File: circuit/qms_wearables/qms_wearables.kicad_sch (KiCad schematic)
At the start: 5 parts, among them P1 SEN-11574, U1 ESP32-DEVKIT-V1, U2 module_mpu6050

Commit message: wip: First draft complete kiosk circuit.
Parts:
- removed Power_Source1: Conn_01x02_Pin, symbol Connector:Conn_01x02_Pin
- removed Vibration_Motor_Module1: Conn_01x03_Pin, symbol Connector:Conn_01x03_Pin
- added BT1: BK-18650-PC4, BK-18650-PC4:BAT_BK-18650-PC4, symbol BK-18650-PC4:BK-18650-PC4
- added P2: PWM VIBRATION MOTOR, SEN_11574:XDCR_SEN-11574, symbol SEN-11574:SEN-11574
- added S1: EG1218, DPST_slide_switch:SW_EG1218, symbol DPST_slide_switch:EG1218
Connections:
- net +3.3V: now also P2.2 (V+)
- net GND: now also BT1.1-, P2.3 (GND)
- net at U1.15 (D23): now also P2.1 (SIGNAL)
- net at U1.17 (VP): no longer P1.1 (SIGNAL)
- net at U1.19 (D34): now also P1.1 (SIGNAL)
- net +5V: no longer names the net of U1.30 (VIN)
- net +5V: now also BT1.2+
- new net: BT1.1+, S1.1
- new net: BT1.2-, S1.2
- no-connect marks 0 -> 1

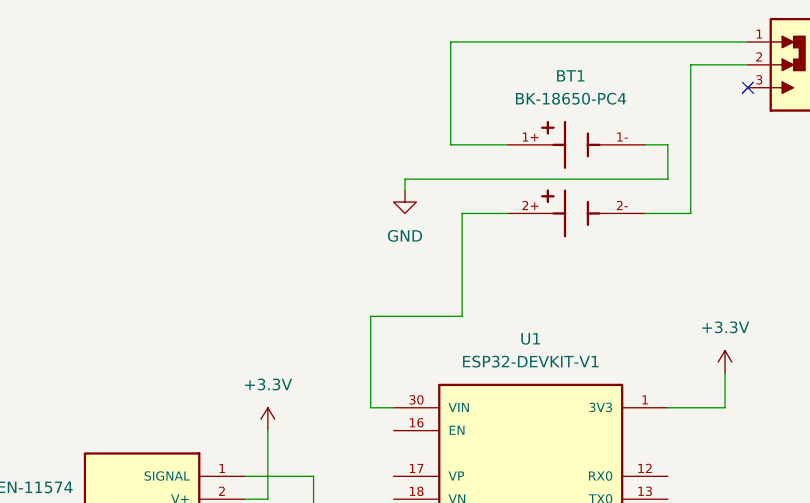
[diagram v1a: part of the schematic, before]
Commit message: wip: First draft complete wearable circuit schematic and pcb with adding 2x battery, DC vibration motor module.
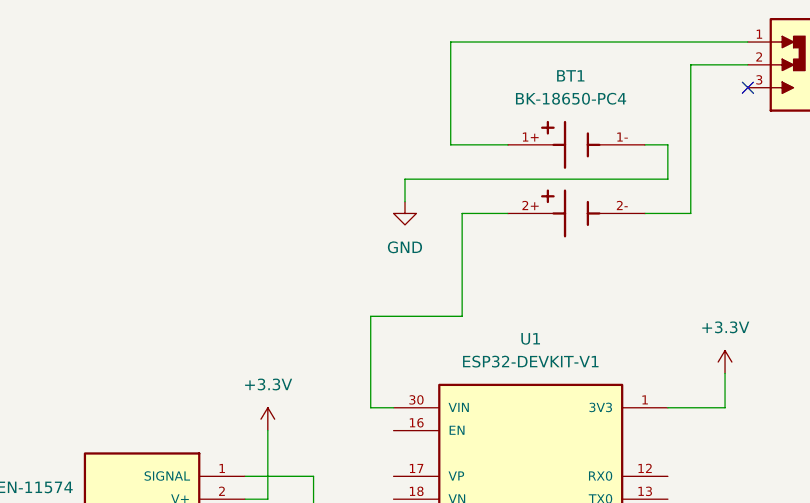
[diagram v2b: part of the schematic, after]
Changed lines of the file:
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@@
 	(wire
 		(pts
-			(xy 105.41 40.64) (xy 105.41 41.91)
+			(xy 105.41 40.64) (xy 105.41 43.18)
 		)
 		(stroke
@@
 	(symbol
 		(lib_id "power:GND")
-		(at 105.41 41.91 0)
+		(at 105.41 43.18 0)
 		(unit 1)
 		(exclude_from_sim no)
@@
 		(fields_autoplaced yes)
 		(property "Reference" "#PWR07"
+			(at 105.41 49.53 0)
+			(effects
+				(font
+					(size 1.27 1.27)
+				)
+				(hide yes)
+			)
+		)
+		(property "Value" "GND"
 			(at 105.41 48.26 0)
 			(effects
@@
 					(size 1.27 1.27)
 				)
-				(hide yes)
-			)
-		)
-		(property "Value" "GND"
-			(at 105.41 46.99 0)
-			(effects
-				(font
-					(size 1.27 1.27)
-				)
 			)
 		)
 		(property "Footprint" ""
-			(at 105.41 41.91 0)
+			(at 105.41 43.18 0)
 			(effects
 				(font
@@
 		)
 		(property "Datasheet" ""
-			(at 105.41 41.91 0)
+			(at 105.41 43.18 0)
 			(effects
 				(font
@@
 		)
 		(property "Description" "Power symbol creates a global label with name \"GND\" , ground"
-			(at 105.41 41.91 0)
-			(effects
-				(font
+			(at 105.41 43.18 0)
+			(effects
+				(font

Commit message: wip: Second draft with replacing the schematic and footprint of vibration motor module
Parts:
- removed P2: PWM VIBRATION MOTOR, SEN_11574:XDCR_SEN-11574, symbol SEN-11574:SEN-11574
- added P2: Vibration Motor Module, Vibration_Motor_Module:XDCR_Vibration_Motor_Module, symbol Vibration_Motor_Module:Vibration_Motor_Module
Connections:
- net +3.3V: now also P2.2 (V+)
- net GND: now also P2.3 (GND)
- net at U1.15 (D23): now also P2.1 (SIGNAL)
- no-connect marks 1 -> 27
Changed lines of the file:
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@@
 	(paper "A4")
 	(no_connect
+		(at 104.14 68.58)
+	)
+	(no_connect
+		(at 104.14 73.66)
+	)
+	(no_connect
+		(at 104.14 99.06)
+	)
+	(no_connect
 		(at 143.51 30.48)
 	)
+	(no_connect
+		(at 134.62 73.66)
+	)
+	(no_connect
+		(at 134.62 76.2)
+	)
+	(no_connect
+		(at 104.14 106.68)
+	)
+	(no_connect
+		(at 134.62 104.14)
+	)
+	(no_connect
+		(at 104.14 93.98)
+	)
+	(no_connect
+		(at 134.62 106.68)
+	)
+	(no_connect
+		(at 104.14 76.2)
+	)
+	(no_connect
+		(at 104.14 104.14)
+	)
+	(no_connect
+		(at 163.83 110.49)
+	)
+	(no_connect
+		(at 134.62 96.52)
+	)
+	(no_connect
+		(at 163.83 107.95)
+	)
+	(no_connect
+		(at 104.14 88.9)
+	)
+	(no_connect
+		(at 134.62 93.98)
+	)
+	(no_connect
+		(at 104.14 91.44)
+	)
+	(no_connect
+		(at 134.62 101.6)
+	)
+	(no_connect
+		(at 163.83 105.41)
+	)
+	(no_connect
+		(at 134.62 81.28)
+	)
+	(no_connect
+		(at 134.62 83.82)
+	)
+	(no_connect
+		(at 104.14 101.6)
+	)
+	(no_connect
+		(at 104.14 109.22)
+	)
+	(no_connect
+		(at 134.62 99.06)
+	)
+	(no_connect
+		(at 104.14 96.52)
+	)
+	(no_connect
+		(at 163.83 113.03)
+	)
 	(wire
 		(pts
@@
 	(wire
 		(pts
-			(xy 80.01 101.6) (xy 83.82 101.6)
+			(xy 77.47 101.6) (xy 83.82 101.6)
 		)
 		(stroke
@@
 	(wire
 		(pts
-			(xy 80.01 99.06) (xy 90.17 99.06)
+			(xy 77.47 99.06) (xy 90.17 99.06)
 		)
 		(stroke
@@
 	(wire
 		(pts
-			(xy 80.01 104.14) (xy 83.82 104.14)
+			(xy 77.47 104.14) (xy 83.82 104.14)
 		)
 		(stroke
@@
 	)
 	(symbol
-		(lib_id "SEN-11574:SEN-11574")
-		(at 74.93 101.6 180)
-		(unit 1)
-		(exclude_from_sim no)
-		(in_bom yes)
-		(on_board yes)
-		(dnp no)
-		(fields_autoplaced yes)
-		(property "Reference" "P2"
-			(at 68.58 91.44 0)
-			(effects
-				(font
-					(size 1.27 1.27)
-				)
-			)
-		)
-		(property "Value" "PWM VIBRATION MOTOR"
-			(at 68.58 93.98 0)
-			(effects
-				(font
-					(size 1.27 1.27)
-				)
-			)
-		)
-		(property "Footprint" "SEN_11574:XDCR_SEN-11574"
-			(at 74.93 101.6 0)
-			(effects
-				(font
-					(size 1.27 1.27)
-				)
-				(justify bottom)
-				(hide yes)
-			)
-		)
-		(property "Datasheet" ""
-			(at 74.93 101.6 0)
-			(effects
-				(font
-					(size 1.27 1.27)
-				)
-				(hide yes)
-			)
-		)
-		(property "Description" ""
-			(at 74.93 101.6 0)
-			(effects
-				(font
-					(size 1.27 1.27)
-				)
-				(hide yes)
-			)
-		)
-		(property "MANUFACTURER" "Sparkfun Electronics"
-			(at 74.93 101.6 0)
-			(effects
-				(font
-					(size 1.27 1.27)
-				)
-				(justify bottom)
-				(hide yes)
-			)
-		)
-		(pin "1"
-		)
-		(pin "3"
-		)
-		(pin "2"
-		)
-		(instances
-			(project "qms_wearables"
-				(path "/81221e85-c470-4436-ab82-7fff3486476b"
-					(reference "P2")
-					(unit 1)
-				)
-			)
-		)
-	)
-	(symbol
 		(lib_id "ESP32-DEVKIT-V1:ESP32-DEVKIT-V1")
 		(at 119.38 91.44 0)
@@
 					(unit 1)
 				)
+			)
+		)
+	)
+	(symbol
+		(lib_id "Vibration_Motor_Module:Vibration_Motor_Module")
+		(at 72.39 101.6 180)
+		(unit 1)
+		(exclude_from_sim no)
+		(in_bom yes)
+		(on_board yes)
+		(dnp no)
+		(fields_autoplaced yes)
+		(property "Reference" "P2"
+			(at 66.04 91.44 0)
+			(effects
+				(font
+					(size 1.27 1.27)
+				)
+			)
+		)
+		(property "Value" "Vibration Motor Module"
+			(at 66.04 93.98 0)
+			(effects
+				(font
+					(size 1.27 1.27)
+				)
+			)
+		)
+		(property "Footprint" "Vibration_Motor_Module:XDCR_Vibration_Motor_Module"
+			(at 64.262 110.49 0)
+			(effects
+				(font
+					(size 1.27 1.27)
+				)
+				(justify bottom)
+				(hide yes)
+			)
+		)
+		(property "Datasheet" ""
+			(at 72.39 101.6 0)
+			(effects
+				(font
+					(size 1.27 1.27)
+				)
+				(hide yes)
+			)
+		)
+		(property "Description" ""
+			(at 72.39 101.6 0)
+			(effects
+				(font
+					(size 1.27 1.27)
+				)
+				(hide yes)
+			)
+		)
+		(property "MANUFACTURER" "Sparkfun Electronics"
+			(at 72.39 101.6 0)
+			(effects
+				(font
+					(size 1.27 1.27)
+				)
+				(justify bottom)
+				(hide yes)
+			)
+		)
+		(pin "1"
+		)
+		(pin "2"
+		)
+		(pin "3"
+		)
+		(instances
+			(project ""
+				(path "/81221e85-c470-4436-ab82-7fff3486476b"
+					(reference "P2")
+					(unit 1)
+				)

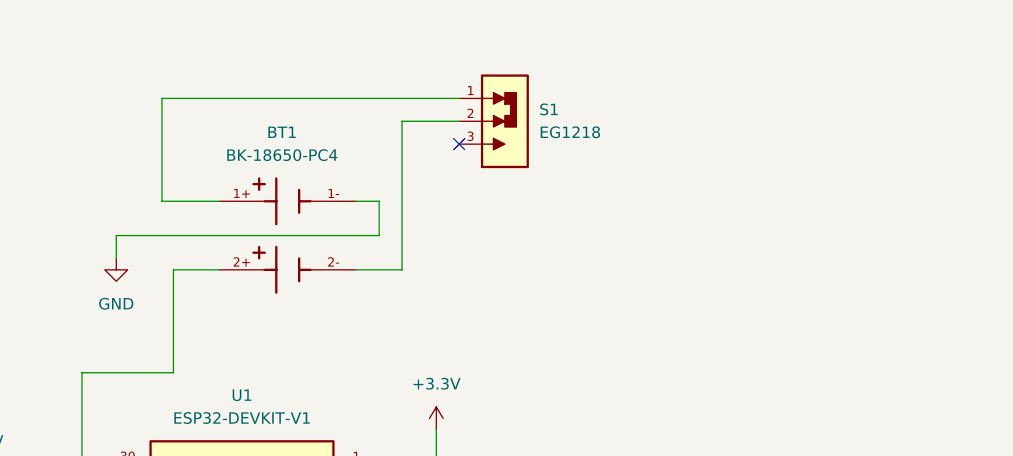
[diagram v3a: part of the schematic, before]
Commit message: wip: Fourth draft with replacing the DPDT Slide Switch and 2 Cell battery footprint and schematic circuit.
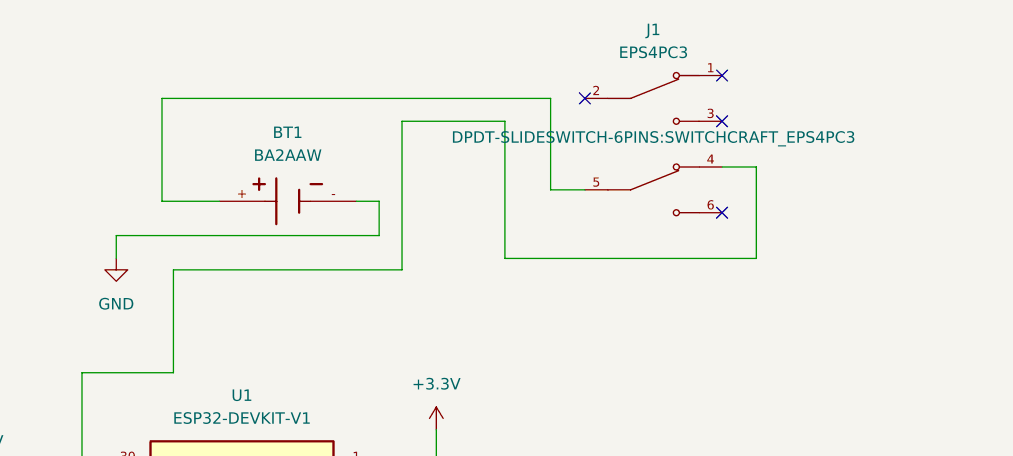
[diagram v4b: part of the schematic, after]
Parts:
- removed BT1: BK-18650-PC4, BK-18650-PC4:BAT_BK-18650-PC4, symbol BK-18650-PC4:BK-18650-PC4
- removed S1: EG1218, DPST_slide_switch:SW_EG1218, symbol DPST_slide_switch:EG1218
- added BT1: BA2AAW, BATTERY-2CELLS-2WIRES:BAT_BA2AAW, symbol BATTERY-2CELLS-2WIRES:BA2AAW
- added J1: EPS4PC3, DPDT-SLIDESWITCH-6PINS:SWITCHCRAFT_EPS4PC3, symbol DPDT-SLIDESWITCH-6PINS:EPS4PC3
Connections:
- net GND: now also BT1.-
- net at U1.30 (VIN): now also J1.4
- new net: BT1.+, J1.5
- no-connect marks 27 -> 30
